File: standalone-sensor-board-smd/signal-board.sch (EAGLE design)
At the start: 7 parts, among them J1 DCJ0202

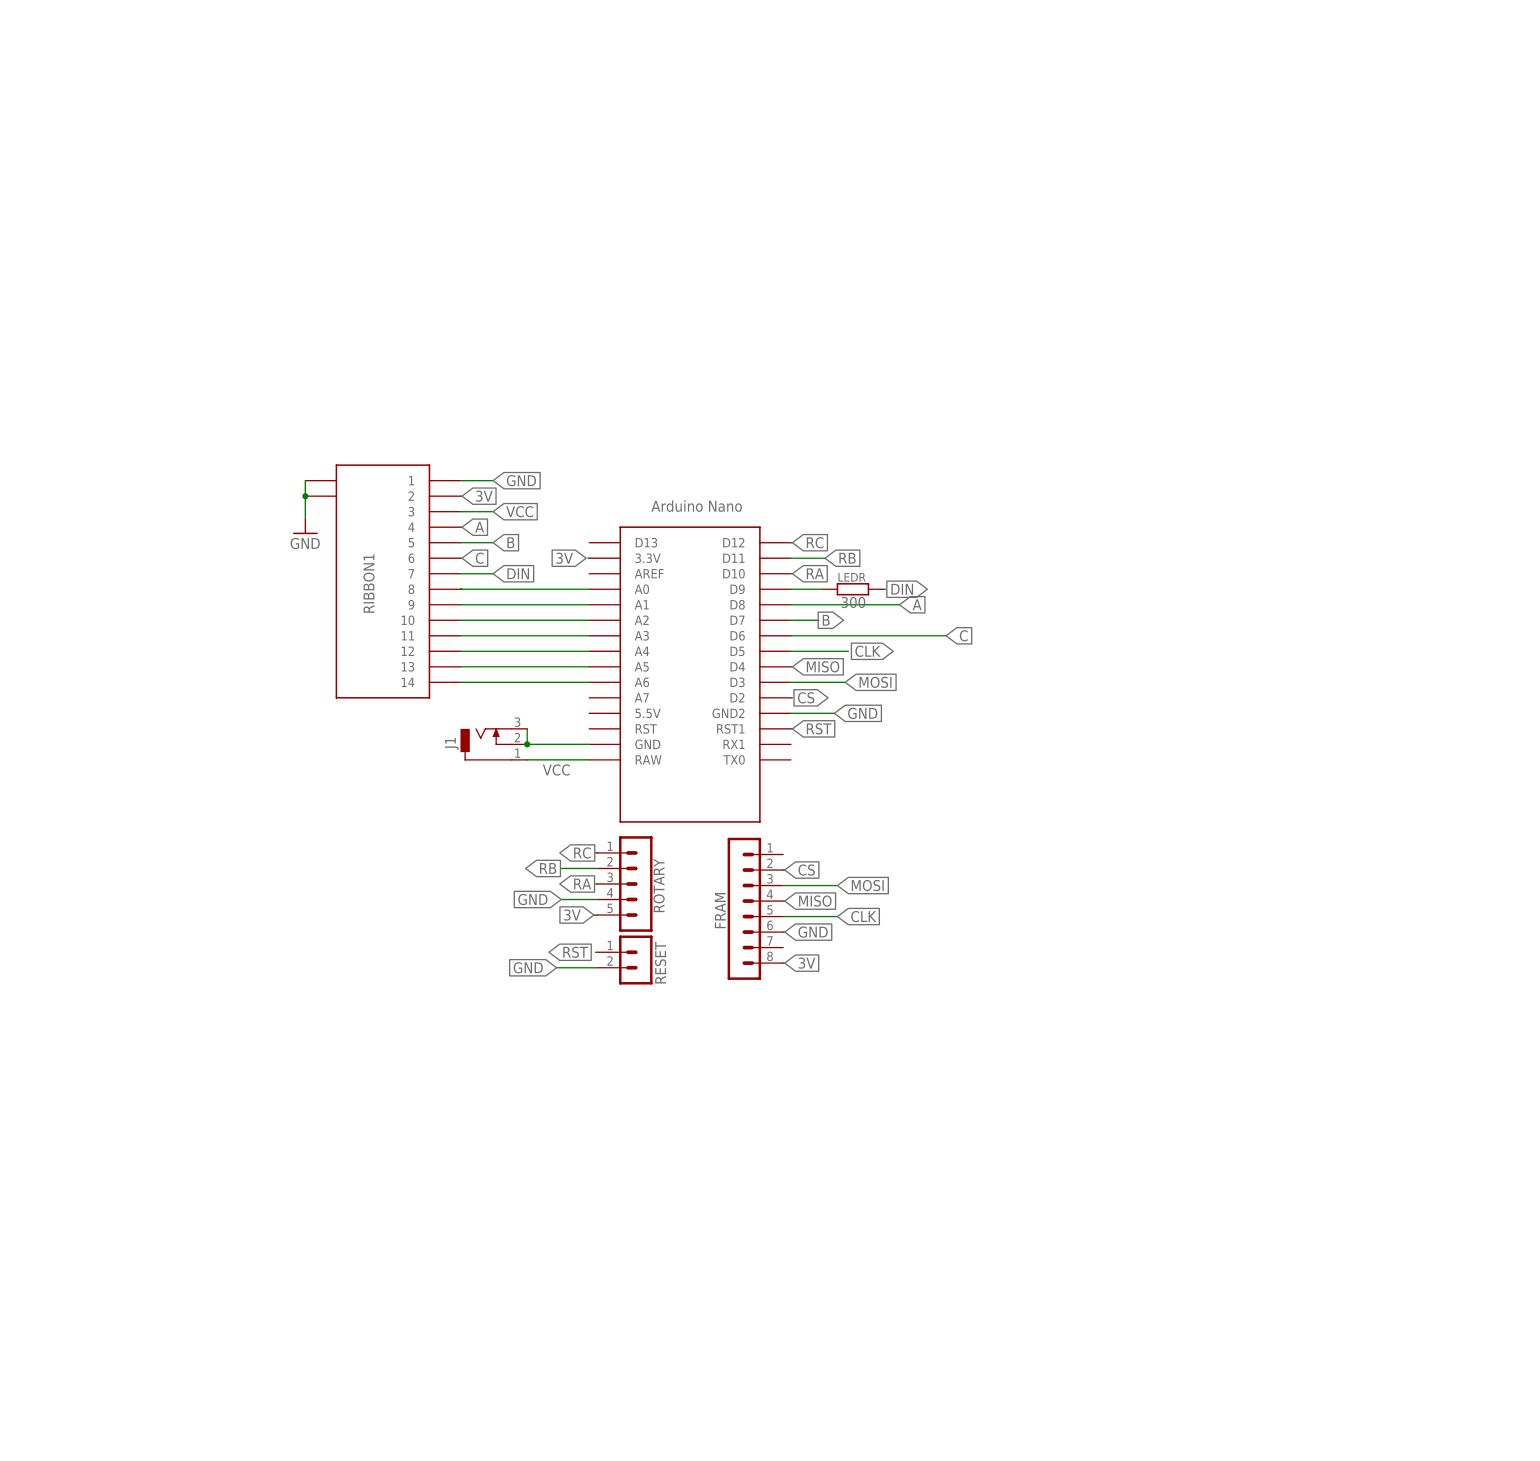
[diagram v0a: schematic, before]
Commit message: init smd version
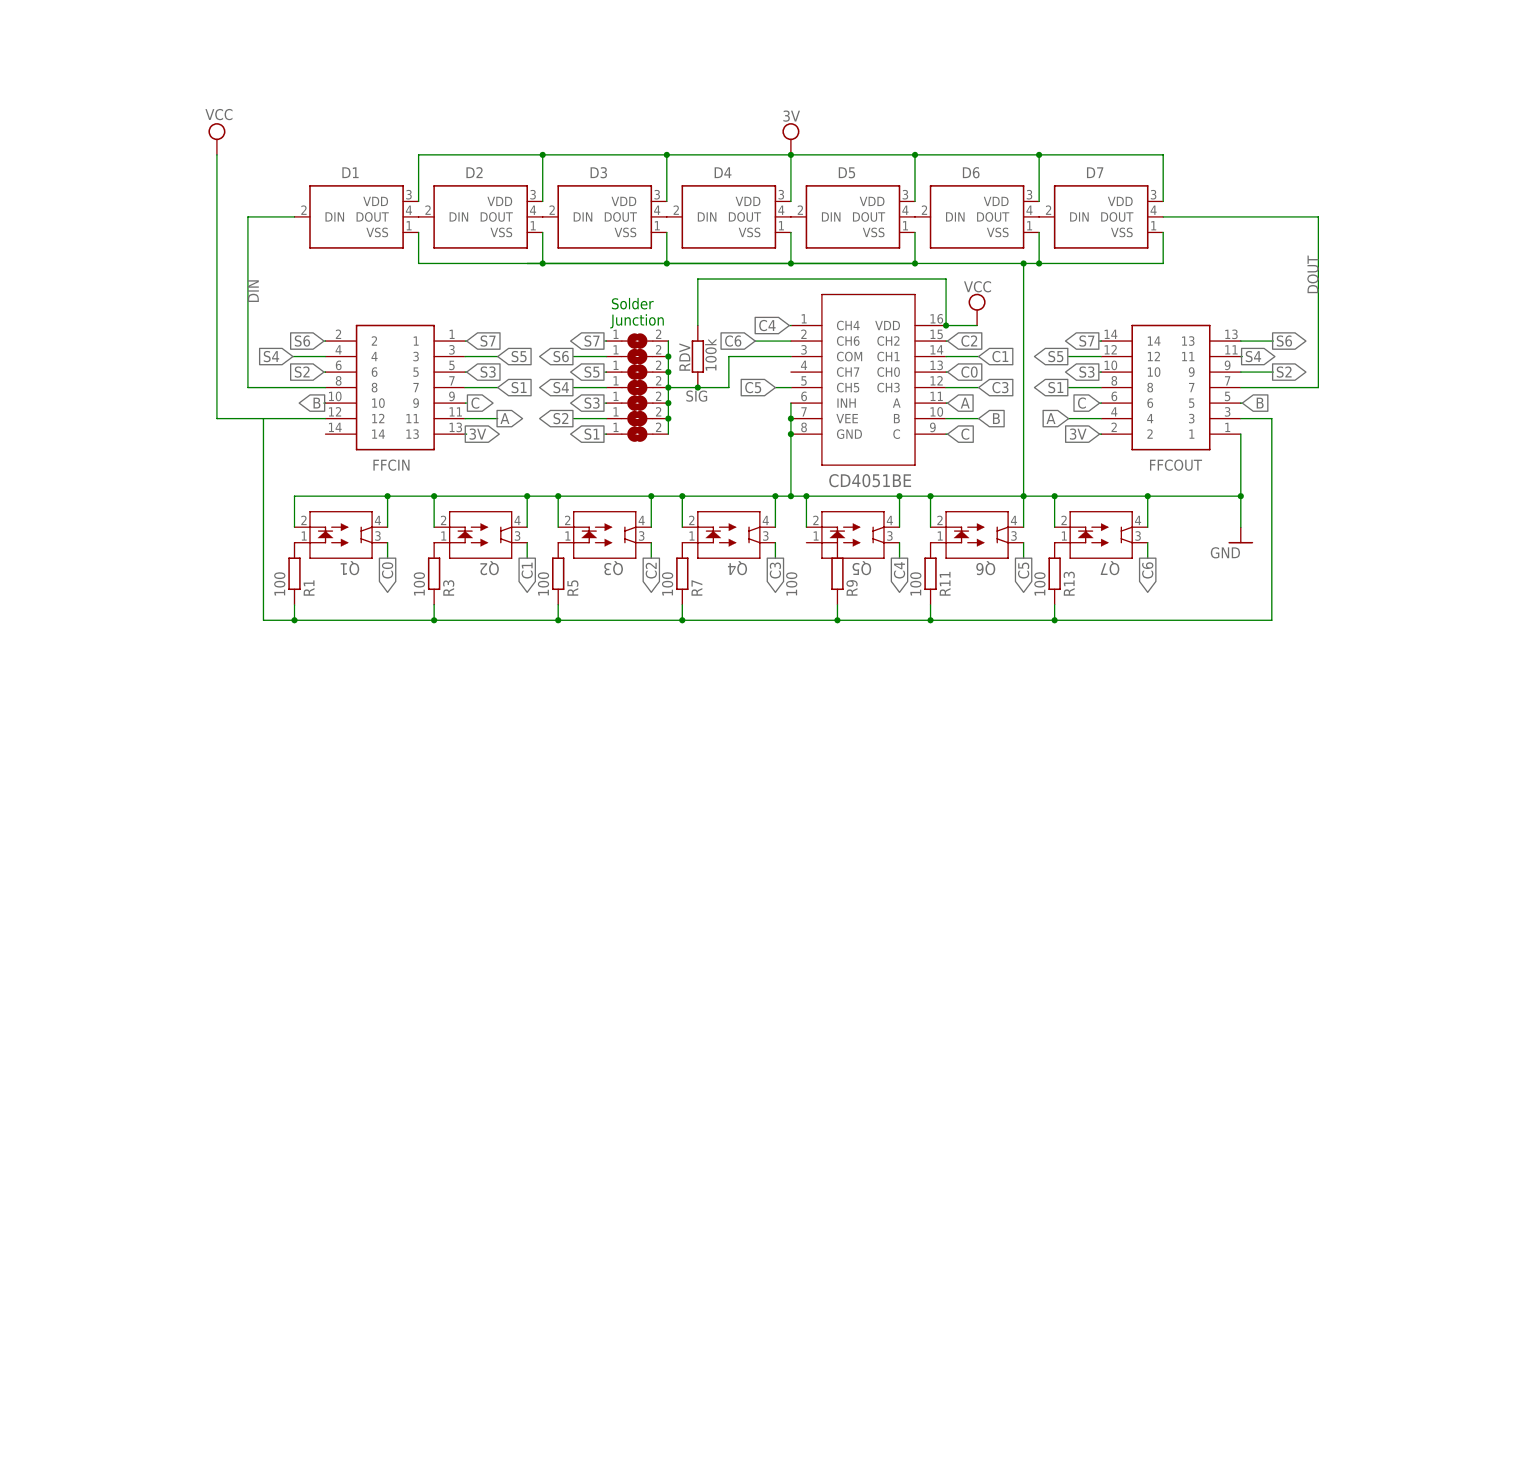
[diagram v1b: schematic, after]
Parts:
- removed FRAM: MB85RS2MTA, con-lstb:MA08-1
- removed J1: DCJ0202, con-jack:DCJ0202
- removed LEDR: 300, rcl:R-EU_0207/10
- removed RESET: B2B-PH-K, con-jst-ph:B2B-PH-K
- removed RIBBON1: (no value), 686114148922:686114148922
- removed ROTARY: B5B-PH-K, con-jst-ph:B5B-PH-K
- removed U$1: NANO, Arduino-clone:NANO
- added D1, D2, D3, D4, D5, D6, D7: 1655, 1655:1655
- added FFCIN, FFCOUT: 52806-1410, 52806-1410:52806-1410
- added Q1, Q2, Q3, Q4, Q5, Q6, Q7: QRE1113, qre1113:QRE1113
- added R1, R11, R13, R3, R5, R7, R9: 100, rcl:R-EU_0207/10
- added RDV: 100k, rcl:R-EU_0207/10
- added SJ1, SJ2, SJ3, SJ4, SJ5, SJ6, SJ7: (no value), jumper:SJ
- added U1: CD4051BE, CD4051BE:CD4051BE
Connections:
- removed net A0: RIBBON1.8, U$1.A0
- removed net A1: RIBBON1.9, U$1.A1
- removed net A2: RIBBON1.10, U$1.A2
- removed net A3: RIBBON1.11, U$1.A3
- removed net A4: RIBBON1.12, U$1.A4
- removed net A5: RIBBON1.13, U$1.A5
- removed net A6: RIBBON1.14, U$1.A6
- removed net CLK: FRAM.5, U$1.D5
- removed net CS: FRAM.2, U$1.D2
- removed net D9: LEDR.1, U$1.D9
- removed net MISO: FRAM.4, U$1.D4
- removed net MOSI: FRAM.3, U$1.D3
- removed net RA: ROTARY.3, U$1.D10
- removed net RB: ROTARY.2, U$1.D11
- removed net RC: ROTARY.1, U$1.D12
- removed net RST: RESET.1, U$1.RST1
- new net C0: Q1.3, U1.CH0
- new net C1: Q2.3, U1.CH1
- new net C2: Q3.3, U1.CH2
- new net C3: Q4.3, U1.CH3
- new net C4: Q5.3, U1.CH4
- new net C5: Q6.3, U1.CH5
- new net C6: Q7.3, U1.CH6
- new net DOUT: D7.DOUT, FFCOUT.7
- new net N$1: Q1.1, R1.2
- new net N$11: Q6.1, R11.2
- new net N$13: Q7.1, R13.2
- new net N$15: D6.DOUT, D7.DIN
- new net N$16: D1.DOUT, D2.DIN
- new net N$17: D2.DOUT, D3.DIN
- new net N$18: D3.DOUT, D4.DIN
- new net N$19: D4.DOUT, D5.DIN
- new net N$2: FFCOUT.3, R1.1, R11.1, R13.1, R3.1, R5.1, R7.1, R9.1
- new net N$20: D5.DOUT, D6.DIN
- new net N$3: Q2.1, R3.2
- new net N$5: Q3.1, R5.2
- new net N$7: Q4.1, R7.2
- new net S1: FFCIN.7, FFCOUT.8, SJ1.1
- new net S2: FFCIN.6, FFCOUT.9, SJ2.1
- new net S3: FFCIN.5, FFCOUT.10, SJ3.1
- new net S4: FFCIN.4, FFCOUT.11, SJ4.1
- new net S5: FFCIN.3, FFCOUT.12, SJ5.1
- new net S6: FFCIN.2, FFCOUT.13, SJ6.1
- new net S7: FFCIN.1, FFCOUT.14, SJ7.1
- new net SIG: RDV.1, SJ1.2, SJ2.2, SJ3.2, SJ4.2, SJ5.2, SJ6.2, SJ7.2, U1.COM
- net 3V: now also D1.VDD, D2.VDD, D3.VDD, D4.VDD, D5.VDD, D6.VDD, D7.VDD, FFCIN.13, FFCOUT.2; no longer FRAM.8, RIBBON1.2, ROTARY.5, U$1.3.3V
- net A: now also FFCIN.11, FFCOUT.4, U1.A; no longer RIBBON1.4, U$1.D8
- net B: now also FFCIN.10, FFCOUT.5, U1.B; no longer RIBBON1.5, U$1.D7
- net C: now also FFCIN.9, FFCOUT.6, U1.C; no longer RIBBON1.6, U$1.D6
- net DIN: now also D1.DIN, FFCIN.8; no longer LEDR.2, RIBBON1.7
- net GND: now also D1.VSS, D2.VSS, D3.VSS, D4.VSS, D5.VSS, D6.VSS, D7.VSS, FFCOUT.1, Q1.2, Q1.4, Q2.2, Q2.4, Q3.2, Q3.4, Q4.2, Q4.4, Q5.2, Q5.4, Q6.2, Q6.4, Q7.2, Q7.4, U1.GND, U1.INH, U1.VEE; no longer FRAM.6, J1.2, J1.3, RESET.2, RIBBON1.1, RIBBON1.MP1, RIBBON1.MP2, ROTARY.4, U$1.GND, U$1.GND2
- net VCC: now also FFCIN.12, RDV.2, U1.VDD; no longer J1.1, RIBBON1.3, U$1.RAW
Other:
- note added: "Solder Junction"

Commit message: add smd boards from standalone
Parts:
- removed D1, D2, D3, D4, D5, D6, D7: 1655, 1655:1655
- removed FFCIN, FFCOUT: 52806-1410, 52806-1410:52806-1410
- removed Q1, Q2, Q3, Q4, Q5, Q6, Q7: QRE1113, qre1113:QRE1113
- removed R1, R11, R13, R3, R5, R7, R9: 100, rcl:R-EU_0207/10
- removed RDV: 100k, rcl:R-EU_0207/10
- added J1: sensors, 686114148922:686114148922
- added J3: to_next_board, 686114148922:686114148922
- added J4: to_controller, 686114148922:686114148922
- added LED1, LED2, LED3, LED4, LED5, LED6, LED7: WS2812B3535, adafruit:WS2812B3535
- added RDV1, RDV2, RDV3, RDV4, RDV5, RDV6, RDV7: 100k, rcl:R-EU_0207/10
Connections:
- removed net N$11: Q6.1, R11.2
- removed net N$13: Q7.1, R13.2
- removed net N$15: D6.DOUT, D7.DIN
- removed net N$16: D1.DOUT, D2.DIN
- removed net N$17: D2.DOUT, D3.DIN
- removed net N$18: D3.DOUT, D4.DIN
- removed net N$19: D4.DOUT, D5.DIN
- removed net N$20: D5.DOUT, D6.DIN
- removed net N$7: Q4.1, R7.2
- new net N$4: LED4.DO, LED5.DI
- new net N$6: LED6.DO, LED7.DI
- net 3V: now also J3.2, J4.13, LED1.VDD, LED2.VDD, LED3.VDD, LED4.VDD, LED5.VDD, LED6.VDD, LED7.VDD; no longer D1.VDD, D2.VDD, D3.VDD, D4.VDD, D5.VDD, D6.VDD, D7.VDD, FFCIN.13, FFCOUT.2
- net A: now also J3.4, J4.11; no longer FFCIN.11, FFCOUT.4
- net B: now also J3.5, J4.10; no longer FFCIN.10, FFCOUT.5
- net C: now also J3.6, J4.9; no longer FFCIN.9, FFCOUT.6
- net C0: now also J1.1, RDV1.2; no longer Q1.3
- net C1: now also J1.2, RDV2.2; no longer Q2.3
- net C2: now also J1.3, RDV3.2; no longer Q3.3
- net C3: now also J1.9, RDV4.2; no longer Q4.3
- net C4: now also J1.10, RDV5.2; no longer Q5.3
- net C5: now also J1.11, RDV6.2; no longer Q6.3
- net C6: now also J1.12, RDV7.2; no longer Q7.3
- net DIN: now also J4.8, LED1.DI; no longer D1.DIN, FFCIN.8
- net DOUT: now also J3.7, LED7.DO; no longer D7.DOUT, FFCOUT.7
- net GND: now also J1.14, J1.MP1, J1.MP2, J3.1, J3.MP1, J3.MP2, J4.14, J4.MP1, J4.MP2, LED1.GND, LED2.GND, LED3.GND, LED4.GND, LED5.GND, LED6.GND, LED7.GND; no longer D1.VSS, D2.VSS, D3.VSS, D4.VSS, D5.VSS, D6.VSS, D7.VSS, FFCOUT.1, Q1.2, Q1.4, Q2.2, Q2.4, Q3.2, Q3.4, Q4.2, Q4.4, Q5.2, Q5.4, Q6.2, Q6.4, Q7.2, Q7.4
- net N$1: now also LED1.DO, LED2.DI; no longer Q1.1, R1.2
- net N$2: now also LED2.DO, LED3.DI; no longer FFCOUT.3, R1.1, R11.1, R13.1, R3.1, R5.1, R7.1, R9.1
- net N$3: now also LED3.DO, LED4.DI; no longer Q2.1, R3.2
- net N$5: now also LED5.DO, LED6.DI; no longer Q3.1, R5.2
- net S1: now also J3.8, J4.7; no longer FFCIN.7, FFCOUT.8
- net S2: now also J3.9, J4.6; no longer FFCIN.6, FFCOUT.9
- net S3: now also J3.10, J4.5; no longer FFCIN.5, FFCOUT.10
- net S4: now also J3.11, J4.4; no longer FFCIN.4, FFCOUT.11
- net S5: now also J3.12, J4.3; no longer FFCIN.3, FFCOUT.12
- net S6: now also J3.13, J4.2; no longer FFCIN.2, FFCOUT.13
- net S7: now also J3.14, J4.1; no longer FFCIN.1, FFCOUT.14
- net SIG: no longer RDV.1
- net VCC: now also J1.13, J3.3, J4.12, RDV1.1, RDV2.1, RDV3.1, RDV4.1, RDV5.1, RDV6.1, RDV7.1; no longer FFCIN.12, RDV.2

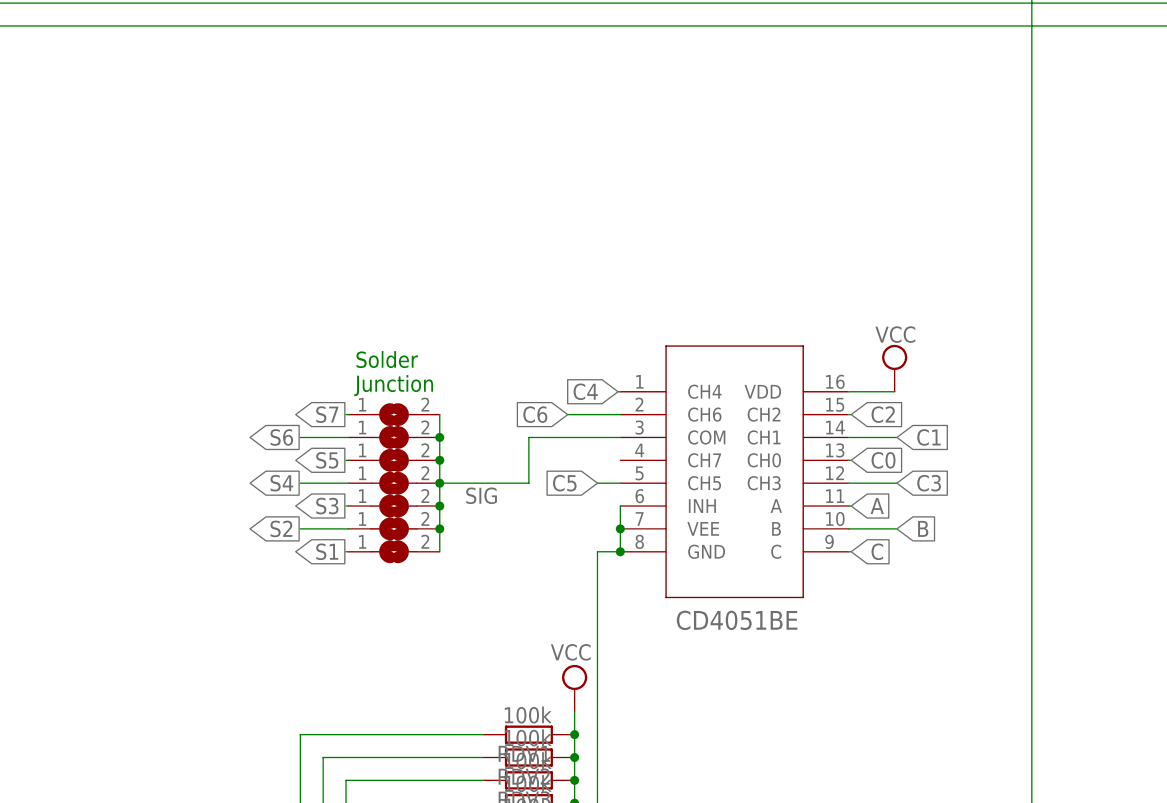
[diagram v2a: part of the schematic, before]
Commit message: add mounting holes
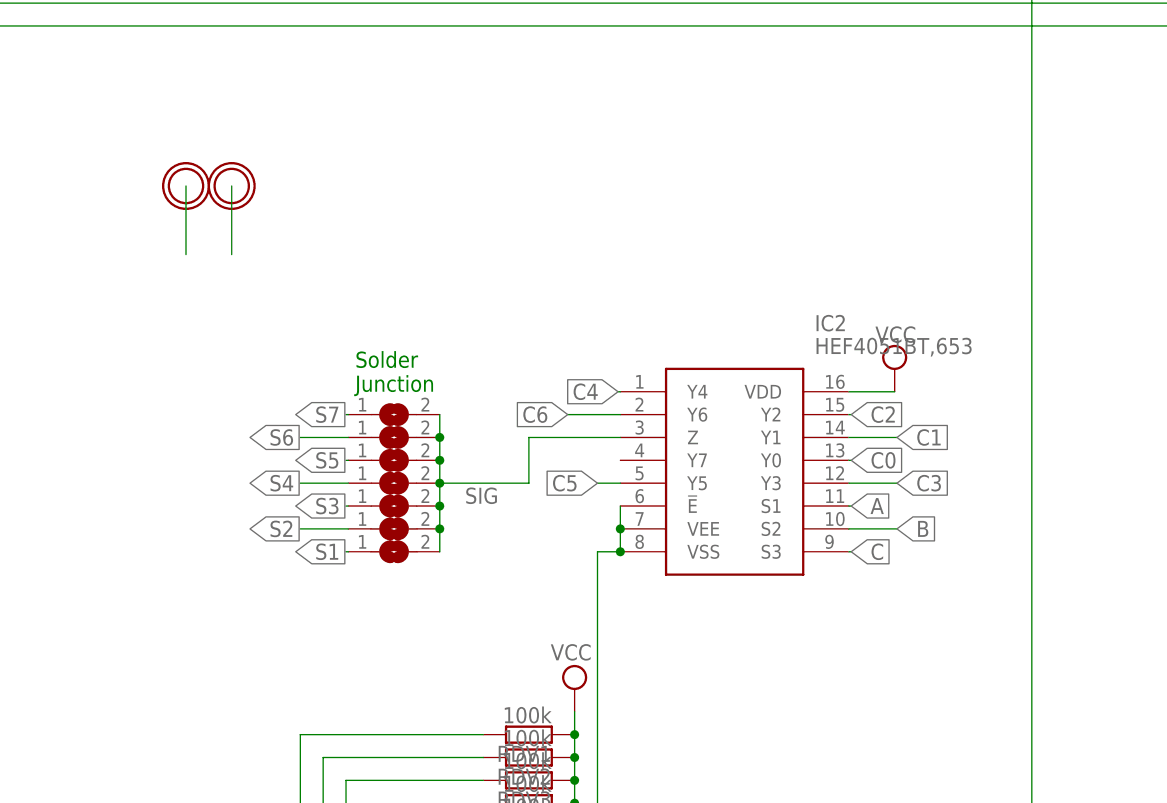
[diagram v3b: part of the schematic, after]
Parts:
- removed U1: CD4051BE, CD4051BE:CD4051BE
- added IC2: HEF4051BT,653, HEF4051BT_653:HEF4051BT,653
- added U$1, U$2: MICROBUILDER_MOUNTINGHOLEMICROBUILDER_MOUNTINGHOL_4.0, microbuilder:MICROBUILDER_MOUNTINGHOLEMICROBUILDER_MOUNTINGHOL_4.0
- RDV1, RDV2, RDV3, RDV4, RDV5, RDV6, RDV7: device rcl:R-EU_0207/10 -> rcl:R-EU_R0805
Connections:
- net A: now also IC2.S1; no longer U1.A
- net B: now also IC2.S2; no longer U1.B
- net C: now also IC2.S3; no longer U1.C
- net C0: now also IC2.Y0; no longer U1.CH0
- net C1: now also IC2.Y1; no longer U1.CH1
- net C2: now also IC2.Y2; no longer U1.CH2
- net C3: now also IC2.Y3; no longer U1.CH3
- net C4: now also IC2.Y4; no longer U1.CH4
- net C5: now also IC2.Y5; no longer U1.CH5
- net C6: now also IC2.Y6; no longer U1.CH6
- net GND: now also IC2.!E, IC2.VEE, IC2.VSS; no longer U1.GND, U1.INH, U1.VEE
- net SIG: now also IC2.Z; no longer U1.COM
- net VCC: now also IC2.VDD; no longer U1.VDD
